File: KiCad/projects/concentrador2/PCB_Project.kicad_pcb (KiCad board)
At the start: 2 copper layers, 91.4 x 88 mm, 43 parts, among them J1 54602-908LF, P1 Grabador, P2 Entrada fuente externa, P4 Header 20X2, P5 Header 2, U1 DSPIC33EP256MC202-I/SP, U2 STEP_DOWN_CONVERTER, U3 LD33V, U4 MAX485, U5 DS3234S#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

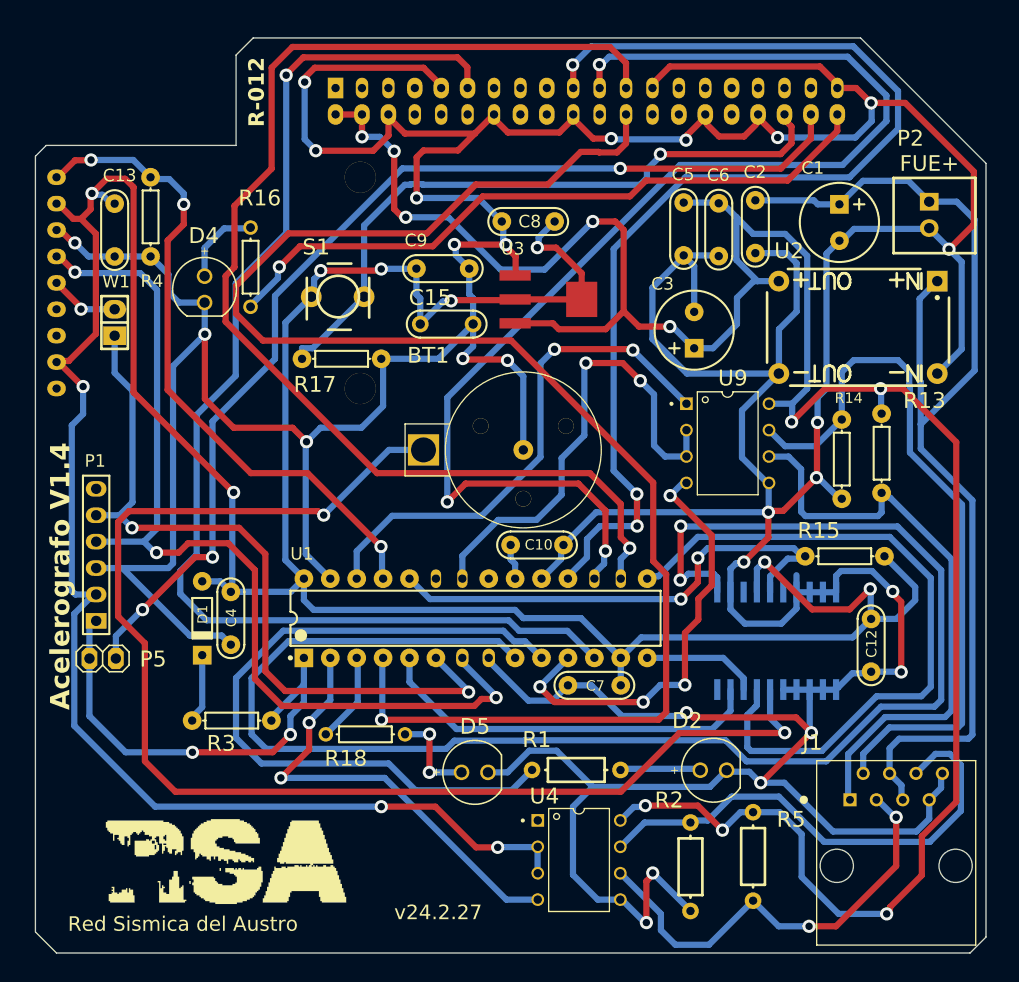
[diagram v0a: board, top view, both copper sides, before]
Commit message: Migracion a SMD
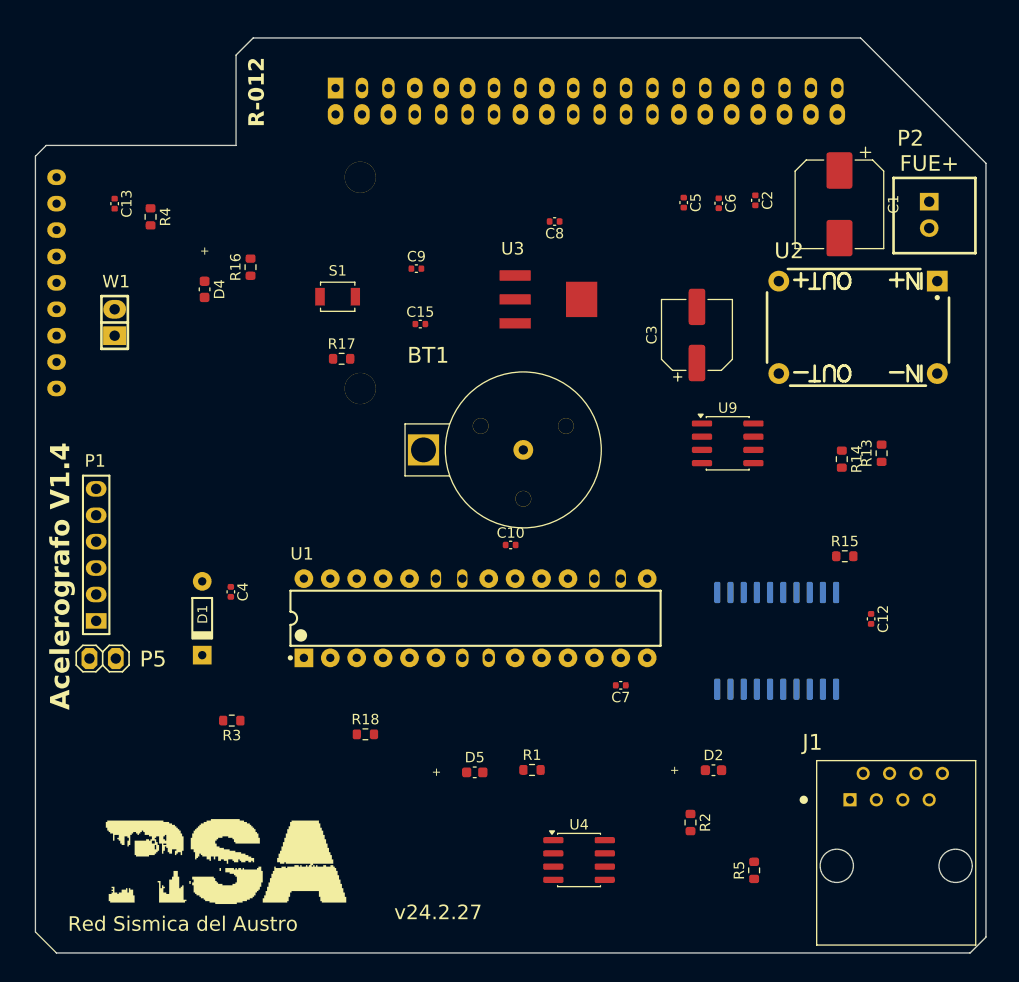
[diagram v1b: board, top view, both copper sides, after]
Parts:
- C1: footprint Propia:C100UFB -> Capacitor_SMD:CP_Elec_8x10
- C10, C12, C13, C15, C2, C4, C5, C6, C7, C8, C9: footprint Propia:RAD0.2 -> Capacitor_SMD:C_0402_1005Metric
- C3: footprint Propia:C100UFB -> Capacitor_SMD:CP_Elec_6.3x7.7
- D2, D4, D5: footprint PcbLib1:Led_Green -> Capacitor_SMD:C_0603_1608Metric
- R1, R2, R5: footprint PcbLib1:4W -> Resistor_SMD:R_0603_1608Metric
- R13, R14, R15, R16, R17, R18, R3, R4: footprint Miscellaneous Devices:AXIAL-0.3 -> Resistor_SMD:R_0603_1608Metric
- S1: footprint Propia:PULSA4 -> Button_Switch_SMD:SW_SPST_B3U-1000P
- U4, U9: footprint PcbLib1:DIP794W47P254L991H457Q8 -> Package_SO:SOIC-8_3.9x4.9mm_P1.27mm
- U5: footprint DS3234S:21-0042B_20 -> Package_SO:SOIC-20W_7.5x12.8mm_P1.27mm
- moved R5 2.92 mm to (171.9, 141.1)
- moved C3 1.31 mm to (166.4, 89.6)
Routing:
- net GND: track 639.0 -> 0.00 mm, vias 26 -> 0
- net VCC: track 341.4 -> 0.00 mm, vias 11 -> 0
- net 5V: track 224.5 -> 0.00 mm, vias 10 -> 0
- net SPI2_DS3234_CS: track 153.3 -> 0.00 mm, vias 2 -> 0
- net SPI1_DSPIC_SS: track 151.9 -> 0.00 mm, vias 1 -> 0
- net NetBT1_0: track 126.5 -> 0.00 mm, vias 2 -> 0
- net SPI1_MISO: track 121.5 -> 0.00 mm, vias 3 -> 0
- net SPI1_SCK: track 117.4 -> 0.00 mm, vias 1 -> 0
- net RPI_INT1: track 117.1 -> 0.00 mm, vias 1 -> 0
- net SPI1_MOSI: track 109.3 -> 0.00 mm, vias 3 -> 0
- net FUENTE_12V: track 106.0 -> 0.00 mm
- net RESET: track 102.4 -> 0.00 mm, vias 3 -> 0
- net DSPIC_TX: track 93.1 -> 0.00 mm, vias 3 -> 0
- net _DSPIC_RX: track 72.6 -> 0.00 mm, vias 2 -> 0
- net INT_SINC_2: track 69.5 -> 0.00 mm
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
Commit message: Fase 4 - Asignación para PCBA
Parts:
- removed BT1: Bateria, Conectores:Bateria-DS1307
- added BT2: Battery, Battery:BatteryHolder_Keystone_500, F.Cu at (143.9, 99.6)
- C1: footprint Capacitor_SMD:CP_Elec_8x10 -> Capacitor_SMD:C_Elec_8x10.2
- C3: footprint Capacitor_SMD:CP_Elec_6.3x7.7 -> Capacitor_SMD:C_Elec_6.3x7.7
- D1: footprint Miscellaneous Devices:DO-35 -> Diode_THT:D_DO-35_SOD27_P7.62mm_Horizontal
- D2, D4, D5: footprint Capacitor_SMD:C_0603_1608Metric -> LED_SMD:LED_0603_1608Metric
- J1: footprint 54602-908LF:*AMPHENOL_54602-908LF -> Connector_RJ:RJ45_Amphenol_54602-x08_Horizontal
- P1: footprint Miscellaneous Connectors:HDR1X6 -> Connector_PinHeader_2.54mm:PinHeader_1x06_P2.54mm_Vertical
- P2: footprint Conectores:MOLEX-2 -> Connector_JST:JST_XH_B2B-XH-A_1x02_P2.50mm_Vertical
- P4: footprint Miscellaneous Connectors_3D:HDR2X20 -> Connector_PinHeader_2.54mm:PinHeader_2x20_P2.54mm_Vertical
- P5: footprint conectores:Header 1X2 -> Connector_PinHeader_2.54mm:PinHeader_1x02_P2.54mm_Vertical
- R1, R14, R16, R17, R18, R2, R3, R4, R5: footprint Resistor_SMD:R_0603_1608Metric -> Resistor_SMD:R_1206_3216Metric
- R13: value Res1 -> 3K3; footprint Resistor_SMD:R_0603_1608Metric -> Resistor_SMD:R_1206_3216Metric
- R15: value Res1 -> 10k; footprint Resistor_SMD:R_0603_1608Metric -> Resistor_SMD:R_1206_3216Metric
- U1: footprint Microchip dsPIC33E:MCHP-SPDIP-SP28 -> Package_DIP:DIP-28_W7.62mm_LongPads
- U3: footprint Footprints:SOT-223 -> Package_TO_SOT_SMD:SOT-223-3_TabPin2
- W1: footprint Propia:SIP-2 -> Connector_PinHeader_2.54mm:PinHeader_1x02_P2.54mm_Vertical
- moved U1 16.7 mm to (129.5, 122.9)
- moved R18 12.3 mm to (145.9, 132.6)
- moved J1 10.1 mm to (179.6, 132.5)
- moved C7 8.80 mm to (159.1, 132.1)
- moved R2 7.51 mm to (161.4, 142.6)
- moved R1 6.38 mm to (154.9, 136.1)
- moved R5 6.18 mm to (165.9, 142.6)
- moved D2 6.18 mm to (163.9, 136.1)
- moved U3 6.12 mm to (154.4, 86.6), turned to 0 degrees
- moved D5 5.97 mm to (148.4, 136.6)
- moved C10 3.03 mm to (151.4, 110.6)
- moved U4 2.50 mm to (154.9, 142.6)
- moved U2 2.33 mm to (191.1, 85.5)
- moved P5 1.99 mm to (108.6, 122.6), turned to 90 degrees
- moved D1 1.92 mm to (116.9, 116.9), turned to 90 degrees
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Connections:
- net D/C renamed D/C
- net NetC10_1 renamed Net-(U1-VCAP)
- net NetD2_1 renamed Net-(D2-A)
- net NetD4_1 renamed Net-(D4-A)
- net NetD5_1 renamed Net-(D5-A)
- D1 pad 1: VCC -> Net-(D1-K)
- D1 pad 2: NetD1_2 -> VCC
- GPS1 pad 5: (no net) -> unconnected-(GPS1-FIX-Pad5)
- GPS1 pad 6: (no net) -> unconnected-(GPS1-VBAT-Pad6)
- GPS1 pad 8: (no net) -> unconnected-(GPS1-3.3V-Pad8)
- P1 pad 6: (no net) -> unconnected-(P1-Pad6)
- P4 pad 1: (no net) -> unconnected-(P4-Pad1)
- P4 pad 10: (no net) -> unconnected-(P4-Pad10)
- P4 pad 12: (no net) -> unconnected-(P4-Pad12)
- P4 pad 15: (no net) -> unconnected-(P4-Pad15)
- P4 pad 16: (no net) -> unconnected-(P4-Pad16)
- P4 pad 17: (no net) -> unconnected-(P4-Pad17)
- P4 pad 18: (no net) -> unconnected-(P4-Pad18)
- P4 pad 22: (no net) -> unconnected-(P4-Pad22)
- P4 pad 27: (no net) -> unconnected-(P4-Pad27)
- P4 pad 28: (no net) -> unconnected-(P4-Pad28)
- P4 pad 3: (no net) -> unconnected-(P4-Pad3)
- P4 pad 32: (no net) -> unconnected-(P4-Pad32)
- P4 pad 33: (no net) -> unconnected-(P4-Pad33)
- P4 pad 35: (no net) -> unconnected-(P4-Pad35)
- P4 pad 5: (no net) -> unconnected-(P4-Pad5)
- P4 pad 7: (no net) -> unconnected-(P4-Pad7)
- P4 pad 8: (no net) -> unconnected-(P4-Pad8)
- R3 pad 2: NetD1_2 -> Net-(D1-K)
- U3 pad 1: 5V -> GND
- U3 pad 2: GND -> VCC
- U3 pad 3: VCC -> 5V
- U4 pad 1: (no net) -> unconnected-(U4-Pad1)
- U5 pad 20: (no net) -> unconnected-(U5-SCLK-Pad20)
- U5 pad 3: (no net) -> unconnected-(U5-32KHZ-Pad3)
- U5 pad 6: (no net) -> unconnected-(U5-RST-Pad6)

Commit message: Fase 4 - 2
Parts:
- C1: value Cap -> 470uF
- C2, C4, C5, C7, C8: value Cap -> 100nF
- C3: value Cap -> 220uF
- C6, C9: value Cap -> 10nF
- D2, D4, D5: value LED3 -> LED_white
- R13, R14, R2, R5: footprint Resistor_SMD:R_1206_3216Metric -> Resistor_SMD:R_0805_2012Metric
- moved P4 0.96 mm to (131.6, 65.5)
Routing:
- net GND: track 0.00 -> 95.9 mm, vias 0 -> 2
- net 5V: track 0.00 -> 2.54 mm

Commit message: Archivos Gerber
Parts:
- moved R18 10.2 mm to (136.1, 129.6)
- moved C8 9.95 mm to (153.7, 88.6)
- moved R14 7.95 mm to (185.5, 107.6), turned to 0 degrees
- moved D5 7.28 mm to (146.4, 129.6)
- moved C13 4.87 mm to (111.8, 81.2)
- moved R16 4.87 mm to (125.9, 87.3)
- moved D4 4.87 mm to (121.5, 89.4)
- moved R17 4.87 mm to (134.6, 96.1)
- moved R4 4.87 mm to (116.3, 82.4)
- moved S1 4.87 mm to (134.3, 90.1)
- moved W1 4.87 mm to (112.8, 93.9)
- moved GPS1 4.85 mm to (107.2, 78.6)
- moved R15 4.84 mm to (185.5, 111.3)
- moved U3 4.54 mm to (155.0, 82.1), turned to 90 degrees
- moved C9 4.54 mm to (143.4, 85.3)
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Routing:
- net GND: track 95.9 -> 517.5 mm, vias 2 -> 1
- net VCC: track 0.00 -> 239.7 mm, vias 0 -> 4
- net 5V: track 2.54 -> 177.9 mm, vias 0 -> 2
- net RESET: track 0.00 -> 113.3 mm, vias 0 -> 1
- net SPI1_MOSI: track 0.00 -> 106.1 mm, vias 0 -> 2
- net RPI_INT1: track 0.38 -> 106.4 mm
- net SPI1_MISO: track 0.00 -> 92.2 mm, vias 0 -> 2
- net FUENTE_12V: track 0.00 -> 85.8 mm
- net SPI1_SCK: track 0.00 -> 85.2 mm, vias 0 -> 2
- net NetBT1_0: track 0.00 -> 85.0 mm, vias 0 -> 1
- net SPI1_DSPIC_SS: track 0.00 -> 72.8 mm
- net DSPIC_TX: track 0.00 -> 70.1 mm
- net _DSPIC_RX: track 0.00 -> 68.1 mm
- net DS3231_SQW: track 0.00 -> 60.6 mm, vias 0 -> 1
- net GPS_1PPS: track 0.00 -> 60.5 mm, vias 0 -> 1
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- added copper zone on B.Cu, net GND
- added copper zone on F.Cu, net GND
